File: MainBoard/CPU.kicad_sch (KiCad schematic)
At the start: 14 parts, among them SW1 ENABLE, SW2 BOOT, U5 ESP32-C3-MINI-1

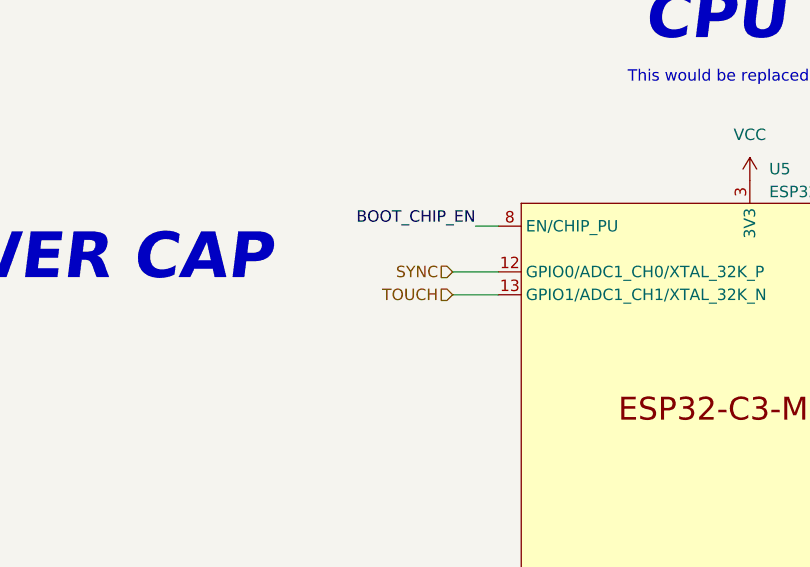
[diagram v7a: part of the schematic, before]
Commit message: clean project, change location of some libraries
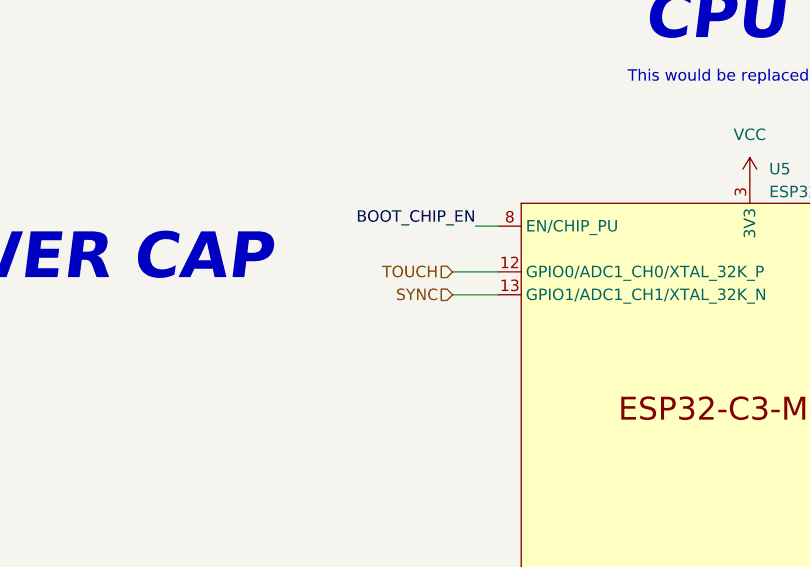
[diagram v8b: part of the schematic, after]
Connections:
- net SYNC: now also U5.13 (GPIO1/ADC1_CH1/XTAL_32K_N); no longer U5.12 (GPIO0/ADC1_CH0/XTAL_32K_P)
- net TOUCH: now also U5.12 (GPIO0/ADC1_CH0/XTAL_32K_P); no longer U5.13 (GPIO1/ADC1_CH1/XTAL_32K_N)
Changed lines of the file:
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@@
 	(hierarchical_label "SYNC"
 		(shape input)
-		(at 92.71 87.63 180)
+		(at 92.71 90.17 180)
 		(effects
 			(font
@@
 	(hierarchical_label "TOUCH"
 		(shape input)
-		(at 92.71 90.17 180)
+		(at 92.71 87.63 180)
 		(effects
 			(font
